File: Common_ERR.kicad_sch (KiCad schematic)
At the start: 6 parts

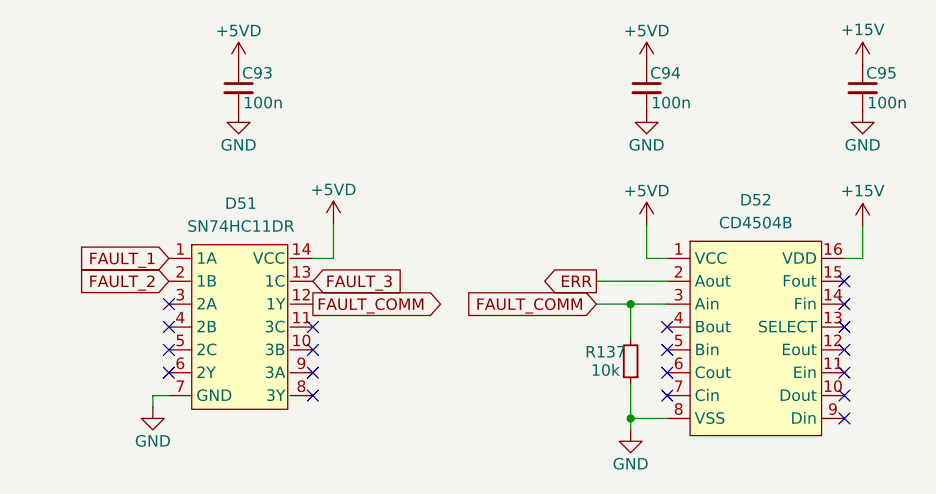
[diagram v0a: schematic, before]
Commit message: Всё влезло, осталься компаратор на NTC
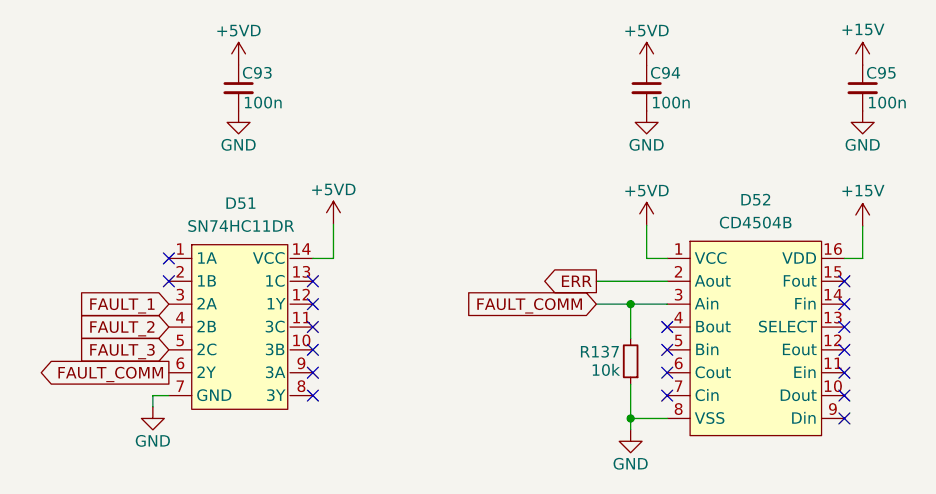
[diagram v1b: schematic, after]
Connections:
- net FAULT_1: now also D51.3 (2A); no longer D51.1 (1A)
- net FAULT_2: now also D51.4 (2B); no longer D51.2 (1B)
- net FAULT_3: now also D51.5 (2C); no longer D51.13 (1C)
- net FAULT_COMM: now also D51.6 (2Y); no longer D51.12 (1Y)
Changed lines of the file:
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@@
   (junction (at 165.862 104.775) (diameter 0) (color 0 0 0 0)
   )
-  (no_connect (at 114.554 107.315))
-  (no_connect (at 114.554 104.775))
   (no_connect (at 130.556 109.855))
   (no_connect (at 130.556 114.935))
   (no_connect (at 130.556 112.395))
-  (no_connect (at 114.554 109.855))
-  (no_connect (at 114.554 112.395))
+  (no_connect (at 130.556 102.235))
+  (no_connect (at 130.556 104.775))
+  (no_connect (at 114.554 102.235))
+  (no_connect (at 114.554 99.695))
   (no_connect (at 130.556 107.315))
   (no_connect (at 189.611 117.475))
@@
     )
   )
-  (global_label "FAULT_3" (shape input) (at 130.556 102.235 0) (fields_autoplaced)
-    (effects (font (size 1.27 1.27)) (justify left))
-    (property "Intersheet References" "${INTERSHEET_REFS}" (id 0) (at 140.6496 102.1556 0)
-      (effects (font (size 1.27 1.27)) (justify left) hide)
-    )
-  )
-  (global_label "FAULT_2" (shape input) (at 114.554 102.235 180) (fields_autoplaced)
-    (effects (font (size 1.27 1.27)) (justify right))
-    (property "Intersheet References" "${INTERSHEET_REFS}" (id 0) (at 104.4604 102.3144 0)
-      (effects (font (size 1.27 1.27)) (justify right) hide)
-    )
-  )
-  (global_label "FAULT_1" (shape input) (at 114.554 99.695 180) (fields_autoplaced)
-    (effects (font (size 1.27 1.27)) (justify right))
-    (property "Intersheet References" "${INTERSHEET_REFS}" (id 0) (at 104.4604 99.7744 0)
+  (global_label "FAULT_3" (shape input) (at 114.554 109.855 180) (fields_autoplaced)
+    (effects (font (size 1.27 1.27)) (justify right))
+    (property "Intersheet References" "${INTERSHEET_REFS}" (id 0) (at 104.4604 109.9344 0)
+      (effects (font (size 1.27 1.27)) (justify right) hide)
+    )
+  )
+  (global_label "FAULT_2" (shape input) (at 114.554 107.315 180) (fields_autoplaced)
+    (effects (font (size 1.27 1.27)) (justify right))
+    (property "Intersheet References" "${INTERSHEET_REFS}" (id 0) (at 104.4604 107.3944 0)
+      (effects (font (size 1.27 1.27)) (justify right) hide)
+    )
+  )
+  (global_label "FAULT_1" (shape input) (at 114.554 104.775 180) (fields_autoplaced)
+    (effects (font (size 1.27 1.27)) (justify right))
+    (property "Intersheet References" "${INTERSHEET_REFS}" (id 0) (at 104.4604 104.8544 0)
       (effects (font (size 1.27 1.27)) (justify right) hide)
     )
@@
     )
   )
-  (global_label "FAULT_COMM" (shape output) (at 130.556 104.775 0) (fields_autoplaced)
-    (effects (font (size 1.27 1.27)) (justify left))
-    (property "Intersheet References" "${INTERSHEET_REFS}" (id 0) (at 144.9434 104.6956 0)
-      (effects (font (size 1.27 1.27)) (justify left) hide)
+  (global_label "FAULT_COMM" (shape output) (at 114.554 112.395 180) (fields_autoplaced)
+    (effects (font (size 1.27 1.27)) (justify right))
+    (property "Intersheet References" "${INTERSHEET_REFS}" (id 0) (at 100.1666 112.4744 0)
+      (effects (font (size 1.27 1.27)) (justify right) hide)
     )
   )
@@
   (symbol (lib_id "Device:R_Small") (at 165.862 111.125 180) (unit 1)
     (in_bom yes) (on_board yes)
-    (property "Reference" "R137" (id 0) (at 163.068 110.109 0))
+    (property "Reference" "R137" (id 0) (at 162.433 110.109 0))
     (property "Value" "10k" (id 1) (at 163.068 112.141 0))
     (property "Footprint" "Resistor_SMD:R_0805_2012Metric_Pad1.20x1.40mm_HandSolder" (id 2) (at 165.862 111.125 0)
